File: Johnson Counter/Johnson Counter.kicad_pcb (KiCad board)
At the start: 2 copper layers, 28 parts, among them J101 USB_A, U201 74HC74, U301 74HC74, U401 74HC74, U501 74HC74

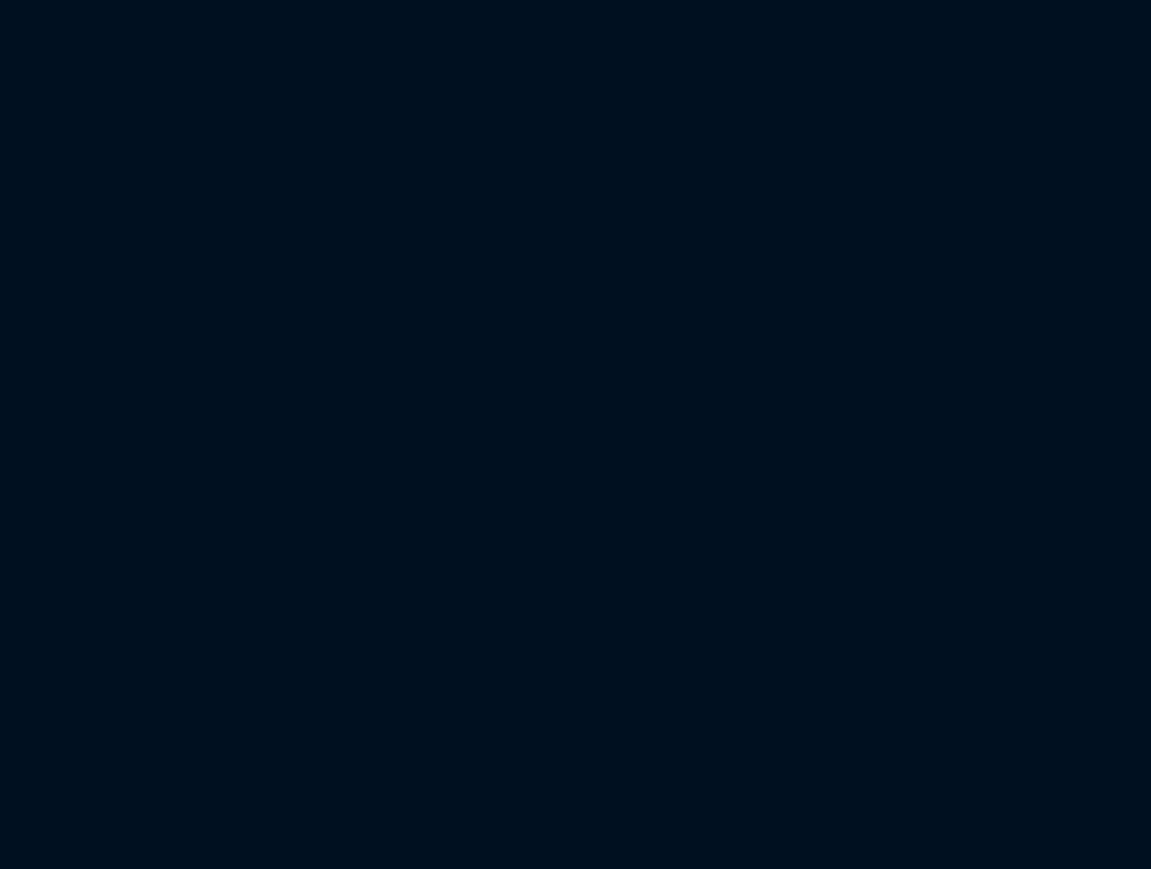
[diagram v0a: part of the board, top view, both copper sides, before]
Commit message: Adding the clock push button
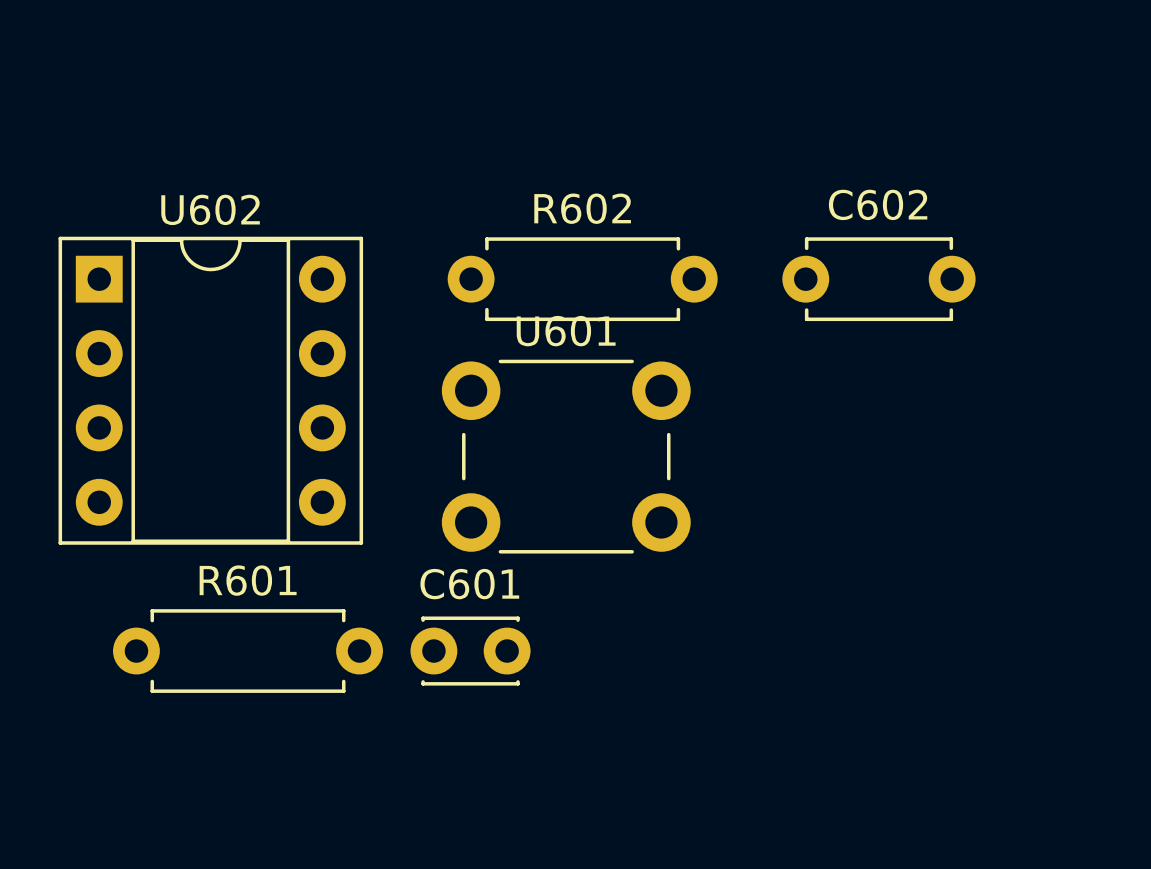
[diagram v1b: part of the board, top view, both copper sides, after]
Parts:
- added C601: 10nF, Capacitor_THT:C_Disc_D3.0mm_W2.0mm_P2.50mm, F.Cu at (77.5, 137.2)
- added C602: 0.1u, Capacitor_THT:C_Disc_D4.7mm_W2.5mm_P5.00mm, F.Cu at (90.2, 124.5)
- added R601: 22k, Resistor_THT:R_Axial_DIN0207_L6.3mm_D2.5mm_P7.62mm_Horizontal, F.Cu at (67.3, 137.2)
- added R602: 1M, Resistor_THT:R_Axial_DIN0207_L6.3mm_D2.5mm_P7.62mm_Horizontal, F.Cu at (78.7, 124.5)
- added U601: SW_Push, Button_Switch_THT:SW_PUSH_6mm_H4.3mm, F.Cu at (78.7, 128.3)
- added U602: LM555xM, Package_DIP:DIP-8_W7.62mm_Socket, F.Cu at (66.0, 124.5)
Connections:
- net /Flipflop 0/CLK renamed /CLOCK
- net /Flipflop 0/D renamed /~{Q_{3}}
- net /Flipflop 0/Q renamed /Q_{0}
- net /Flipflop 0/~{Q} renamed /~{Q_{0}}
- net /Flipflop 1/Q renamed /Q_{1}
- net /Flipflop 1/~{Q} renamed /~{Q_{1}}
- net /Flipflop 2/Q renamed /Q_{2}
- net /Flipflop 2/~{Q} renamed /~{Q_{2}}
- net /Flipflop 3/Q renamed /Q_{3}

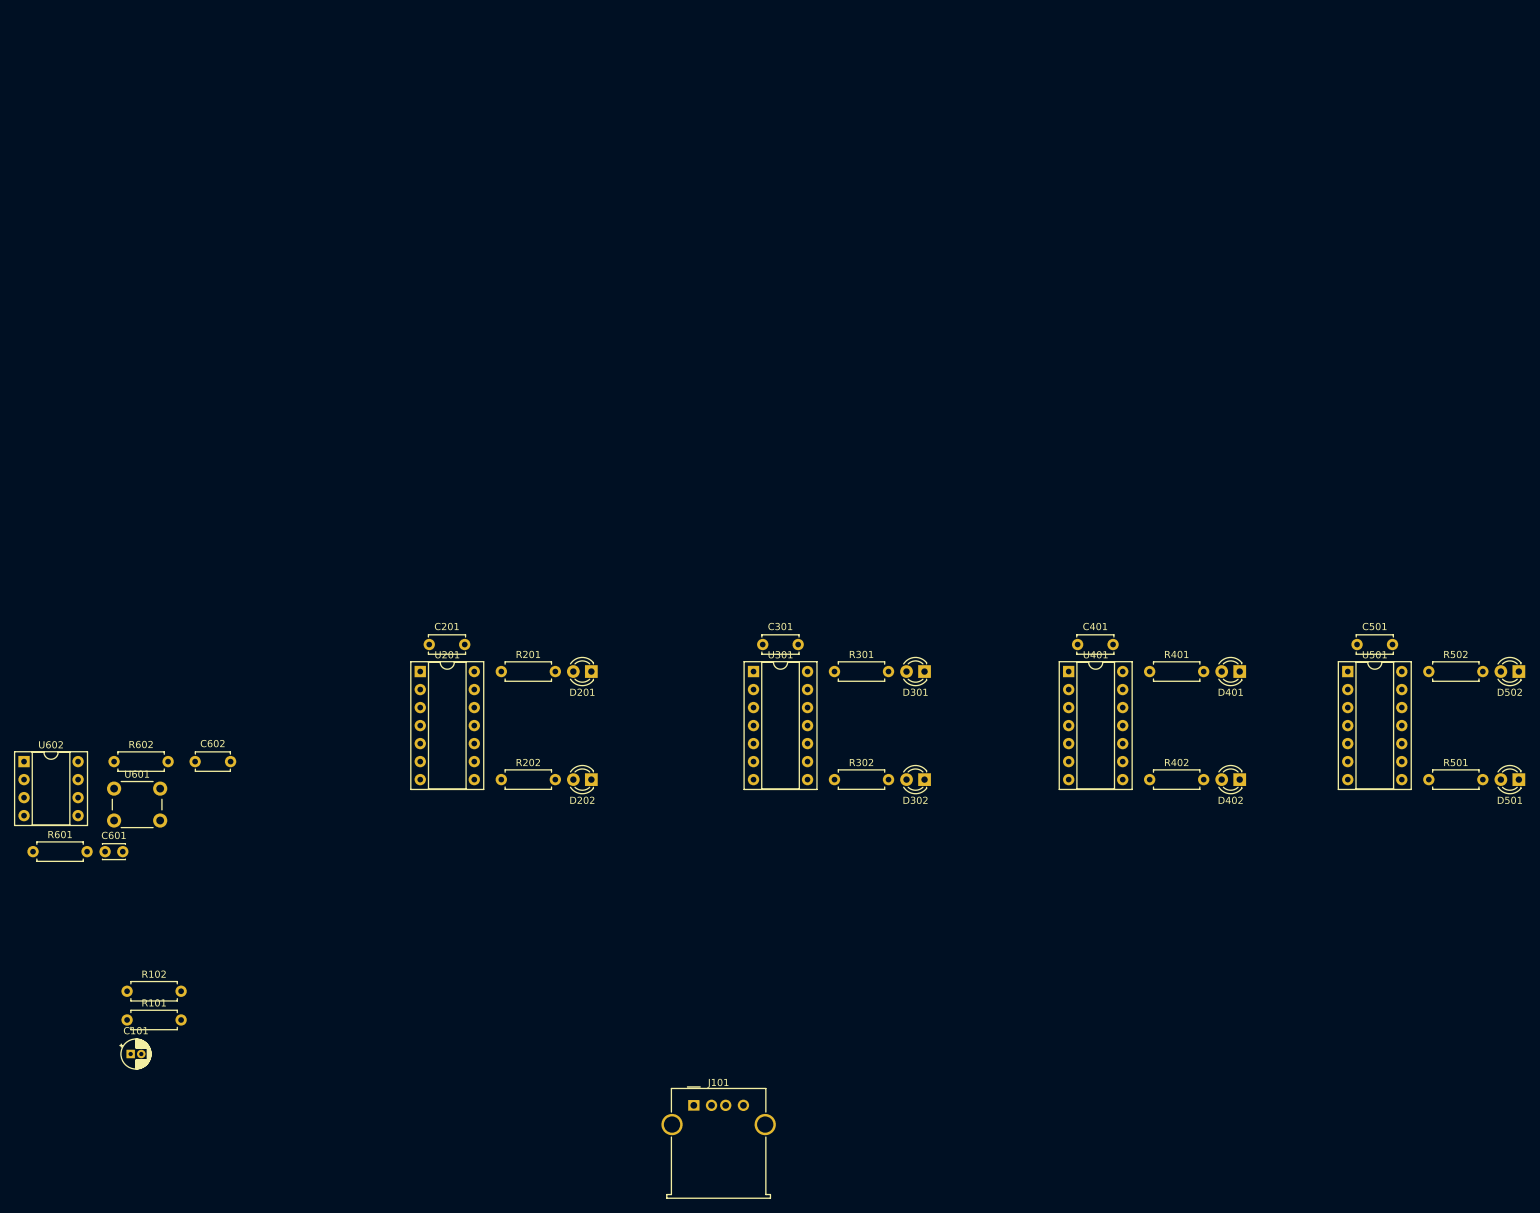
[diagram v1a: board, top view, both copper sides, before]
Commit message: Getting flipflop board locations worked out
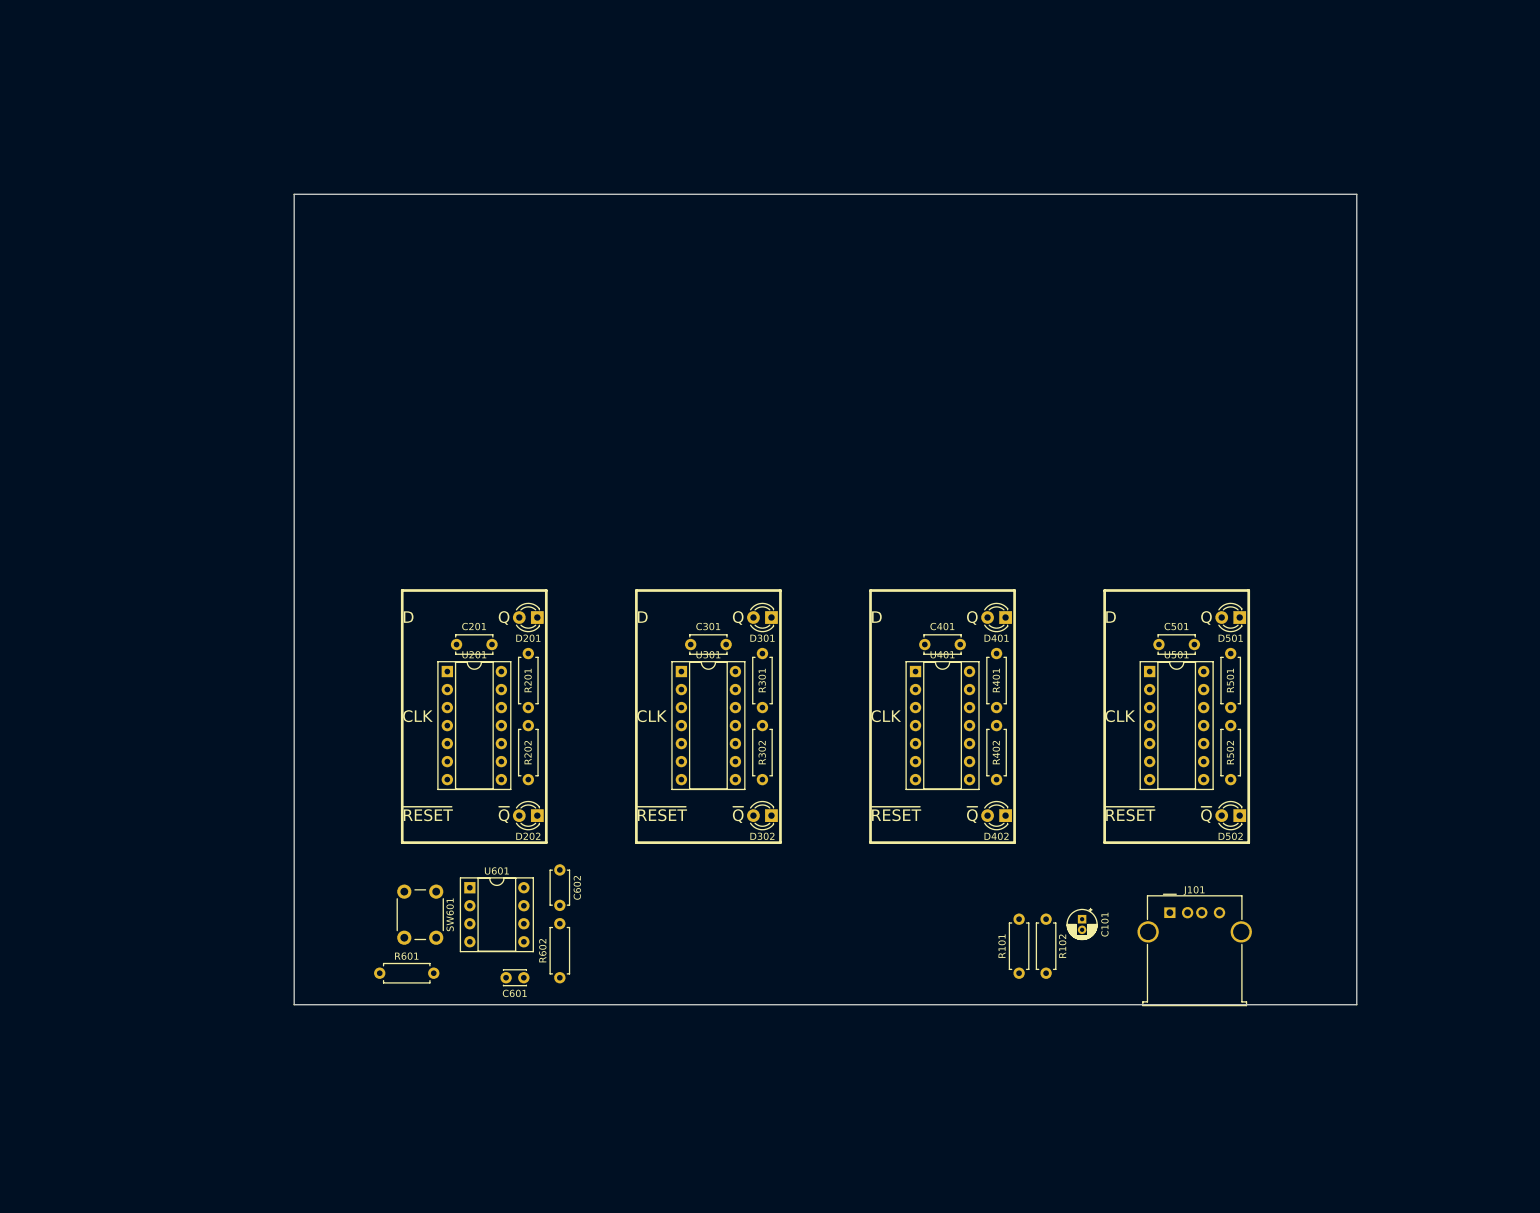
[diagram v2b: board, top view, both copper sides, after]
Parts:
- moved C101 135.5 mm to (215.3, 146.7), turned to -90 degrees
- moved R102 130.0 mm to (210.2, 146.7), turned to -90 degrees
- moved R101 126.0 mm to (206.4, 154.3), turned to 90 degrees
- moved J101 72.4 mm to (227.6, 145.8)
- moved R602 69.9 mm to (141.6, 154.9), turned to 90 degrees
- moved U601 65.3 mm to (128.9, 142.2)
- moved C601 61.7 mm to (136.5, 154.9), turned to 180 degrees
- moved C602 53.7 mm to (141.6, 139.7), turned to -90 degrees
- moved R601 51.8 mm to (116.2, 154.3)
- moved SW601 47.7 mm to (124.2, 142.8), turned to -90 degrees
- moved D501 45.5 mm to (237.5, 104.1)
- moved D502 44.3 mm to (237.5, 132.1)
- moved D401 33.9 mm to (204.5, 104.1)
- moved D402 33.4 mm to (204.5, 132.1)
- moved R501 29.7 mm to (236.2, 116.8), turned to 90 degrees
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- renumbered U601 to SW601, U602 to U601
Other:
- board outline added: 149.9 x 114.3 mm
- board text added: "CLK"
- board text added: "D"
- board text added: "Q"
- board text added: "~{Q}"
- board text added: "~{RESET}"

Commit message: Working on decoder stage
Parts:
- added D701: LED, LED_THT:LED_D5.0mm, F.Cu at (125.7, 68.6)
- added D702: LED, LED_THT:LED_D5.0mm, F.Cu at (141.0, 68.6)
- added D703: LED, LED_THT:LED_D5.0mm, F.Cu at (156.2, 68.6)
- added D704: LED, LED_THT:LED_D5.0mm, F.Cu at (171.4, 68.6)
- added D705: LED, LED_THT:LED_D5.0mm, F.Cu at (186.7, 68.6)
- added D706: LED, LED_THT:LED_D5.0mm, F.Cu at (201.9, 68.6)
- added D707: LED, LED_THT:LED_D5.0mm, F.Cu at (217.2, 68.6)
- added D708: LED, LED_THT:LED_D5.0mm, F.Cu at (232.4, 68.6)
- added R701: 4k7, Resistor_THT:R_Axial_DIN0207_L6.3mm_D2.5mm_P7.62mm_Horizontal, F.Cu at (125.7, 52.1)
- added R702: 4k7, Resistor_THT:R_Axial_DIN0207_L6.3mm_D2.5mm_P7.62mm_Horizontal, F.Cu at (130.8, 52.1)
- added R703: 4k7, Resistor_THT:R_Axial_DIN0207_L6.3mm_D2.5mm_P7.62mm_Horizontal, F.Cu at (166.4, 52.1)
- added R704: 4k7, Resistor_THT:R_Axial_DIN0207_L6.3mm_D2.5mm_P7.62mm_Horizontal, F.Cu at (171.4, 52.1)
- added R705: 4k7, Resistor_THT:R_Axial_DIN0207_L6.3mm_D2.5mm_P7.62mm_Horizontal, F.Cu at (186.7, 52.1)
- added R706: 4k7, Resistor_THT:R_Axial_DIN0207_L6.3mm_D2.5mm_P7.62mm_Horizontal, F.Cu at (191.8, 52.1)
- added R707: 4k7, Resistor_THT:R_Axial_DIN0207_L6.3mm_D2.5mm_P7.62mm_Horizontal, F.Cu at (227.3, 52.1)
- added R708: 4k7, Resistor_THT:R_Axial_DIN0207_L6.3mm_D2.5mm_P7.62mm_Horizontal, F.Cu at (232.4, 52.1)
- added U701: 4081, Package_DIP:DIP-14_W7.62mm_Socket, F.Cu at (141.0, 59.7)
- added U702: 4081, Package_DIP:DIP-14_W7.62mm_Socket, F.Cu at (201.9, 59.7)
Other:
- board text added: "Q_{0}"
- board text added: "Q_{1}"
- board text added: "Q_{2}"
- board text added: "Q_{3}"
- board text removed: "Q"

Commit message: Routing...
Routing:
- net /~{Q_{3}}: track 0.00 -> 297.1 mm, vias 0 -> 2
- net /Q_{2}: track 0.00 -> 276.3 mm, vias 0 -> 5
- net /Q_{0}: track 0.00 -> 254.7 mm, vias 0 -> 5
- net /Q_{1}: track 0.00 -> 230.2 mm, vias 0 -> 5
- net /~{Q_{1}}: track 0.00 -> 189.3 mm, vias 0 -> 3
- net /~{Q_{0}}: track 0.00 -> 183.9 mm, vias 0 -> 3
- net /~{Q_{2}}: track 0.00 -> 177.3 mm, vias 0 -> 3
- net /~{RESET}: track 0.00 -> 122.4 mm
- net /Q_{3}: track 0.00 -> 121.5 mm, vias 0 -> 2
- net /CLOCK: track 0.00 -> 121.5 mm
- net Net-(R708-Pad1): track 0.00 -> 28.5 mm
- net Net-(R704-Pad1): track 0.00 -> 28.1 mm
- net Net-(R705-Pad1): track 0.00 -> 27.6 mm
- net Net-(U701-Pad3): track 0.00 -> 27.6 mm
- net Net-(R702-Pad1): track 0.00 -> 25.1 mm
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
